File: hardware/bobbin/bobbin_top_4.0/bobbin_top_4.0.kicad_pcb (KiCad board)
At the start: 2 copper layers, 90.5 x 8.5 mm, 1 part

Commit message: new scheme
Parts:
- H3: footprint cycfi_library:single-pad-10x2 -> cycfi_library:xr2-4.0-bobbin-top
- moved H3 2.60 mm to (134.0, 65.0)
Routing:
- net GND: track 0.00 -> 2.70 mm, vias 2 -> 1
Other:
- outline, holes or cut-outs redrawn
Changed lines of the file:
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@@
   (general
     (thickness 1.6)
-    (drawings 20)
+    (drawings 12)
     (tracks 2)
     (zones 0)
@@
     (44 Edge.Cuts user)
     (45 Margin user)
-    (46 B.CrtYd user hide)
-    (47 F.CrtYd user hide)
-    (48 B.Fab user hide)
-    (49 F.Fab user hide)
+    (46 B.CrtYd user)
+    (47 F.CrtYd user)
+    (48 B.Fab user)
+    (49 F.Fab user)
   )
   (setup
@@
     (add_net GND)
   )
-  (module cycfi_library:single-pad-10x2 (layer F.Cu)
-    (at 134 62.4)
-    (fp_text reference H3 (at 6.5 0.1) (layer F.SilkS) hide
+  (module cycfi_library:xr2-4.0-bobbin-top (layer F.Cu)
+    (at 134 65)
+    (fp_text reference H3 (at 0 6) (layer F.SilkS)
       (effects (font (size 1 1) (thickness 0.15)))
     )
-    (fp_text value single_pad_smd (at 0 -2.54) (layer F.Fab)
+    (fp_text value single_pad_smd (at 0 -4) (layer F.Fab)
       (effects (font (size 1 1) (thickness 0.15)))
     )
-    (pad 1 smd rect (at 0 0) (size 10 2) (layers F.Cu F.Paste F.Mask)
+    (pad 1 thru_hole oval (at 0 0) (size 84.5 2.5) (drill oval 84 2) (layers *.Cu *.Mask)
       (net 1 GND))
   )
-  (gr_line (start 129 61.4) (end 129 63.4) (layer Dwgs.User) (width 0.05))
-  (gr_line (start 129 63.4) (end 139 63.4) (layer Dwgs.User) (width 0.05))
-  (gr_line (start 139 63.4) (end 139 61.4) (layer Dwgs.User) (width 0.05))
-  (gr_line (start 139 61.4) (end 129 61.4) (layer Dwgs.User) (width 0.05))
   (gr_arc (start 175 65) (end 175 69.25) (angle -180) (layer Edge.Cuts) (width 0.05))
-  (gr_line (start 175 64) (end 175 66) (layer Edge.Cuts) (width 0.05))
-  (gr_line (start 93 66) (end 175 66) (layer Edge.Cuts) (width 0.05))
-  (gr_line (start 93 64) (end 93 66) (layer Edge.Cuts) (width 0.05))
-  (gr_line (start 93 64) (end 175 64) (layer Edge.Cuts) (width 0.05))
   (gr_line (start 175 69.25) (end 93 69.25) (layer Edge.Cuts) (width 0.05))
   (gr_line (start 93 60.75) (end 175 60.75) (layer Edge.Cuts) (width 0.05))
   (gr_arc (start 93 65) (end 93 60.75) (angle -180) (layer Edge.Cuts) (width 0.05))
-  (gr_line (start 93 64) (end 93 66) (layer Dwgs.User) (width 0.05))
-  (gr_line (start 175 64) (end 175 66) (layer Dwgs.User) (width 0.05))
-  (gr_line (start 93 66) (end 175 66) (layer Dwgs.User) (width 0.05))
-  (gr_line (start 93 64) (end 175 64) (layer Dwgs.User) (width 0.05))
+  (gr_line (start 104 64) (end 104 66) (layer Dwgs.User) (width 0.05))
+  (gr_line (start 164 64) (end 164 66) (layer Dwgs.User) (width 0.05))
+  (gr_line (start 104 66) (end 164 66) (layer Dwgs.User) (width 0.05))
+  (gr_line (start 104 64) (end 164 64) (layer Dwgs.User) (width 0.05))
   (gr_line (start 175 69.25) (end 93 69.25) (layer Dwgs.User) (width 0.05))
   (gr_line (start 93 60.75) (end 175 60.75) (layer Dwgs.User) (width 0.05))
   (gr_arc (start 93 65) (end 93 60.75) (angle -180) (layer Dwgs.User) (width 0.05))
   (gr_arc (start 175 65) (end 175 69.25) (angle -180) (layer Dwgs.User) (width 0.05))
-  (via (at 128 62.5) (size 0.8) (drill 0.4) (layers F.Cu B.Cu) (net 1))
-  (via (at 140 62.5) (size 0.8) (drill 0.4) (layers F.Cu B.Cu) (net 1))
+  (via (at 134 62.3) (size 0.8) (drill 0.4) (layers F.Cu B.Cu) (net 1))
+  (segment (start 134 62.3) (end 134 65) (width 0.25) (layer B.Cu) (net 1))
   (zone (net 1) (net_name GND) (layer F.Cu) (hatch edge 0.508)
     (connect_pads yes (clearance 0.25))
@@
     (polygon
       (pts
-        (xy 180 70) (xy 88 70) (xy 88 60) (xy 180 60)
+        (xy 179.3 69.9) (xy 88.7 70) (xy 88.7 60) (xy 179.3 59.9)
       )
     )
@@
     (polygon
       (pts
-        (xy 180 70) (xy 88 70) (xy 88 60) (xy 180 60)
+        (xy 179.3 69.9) (xy 88.7 70) (xy 88.7 60) (xy 179.3 59.9)
       )
     )

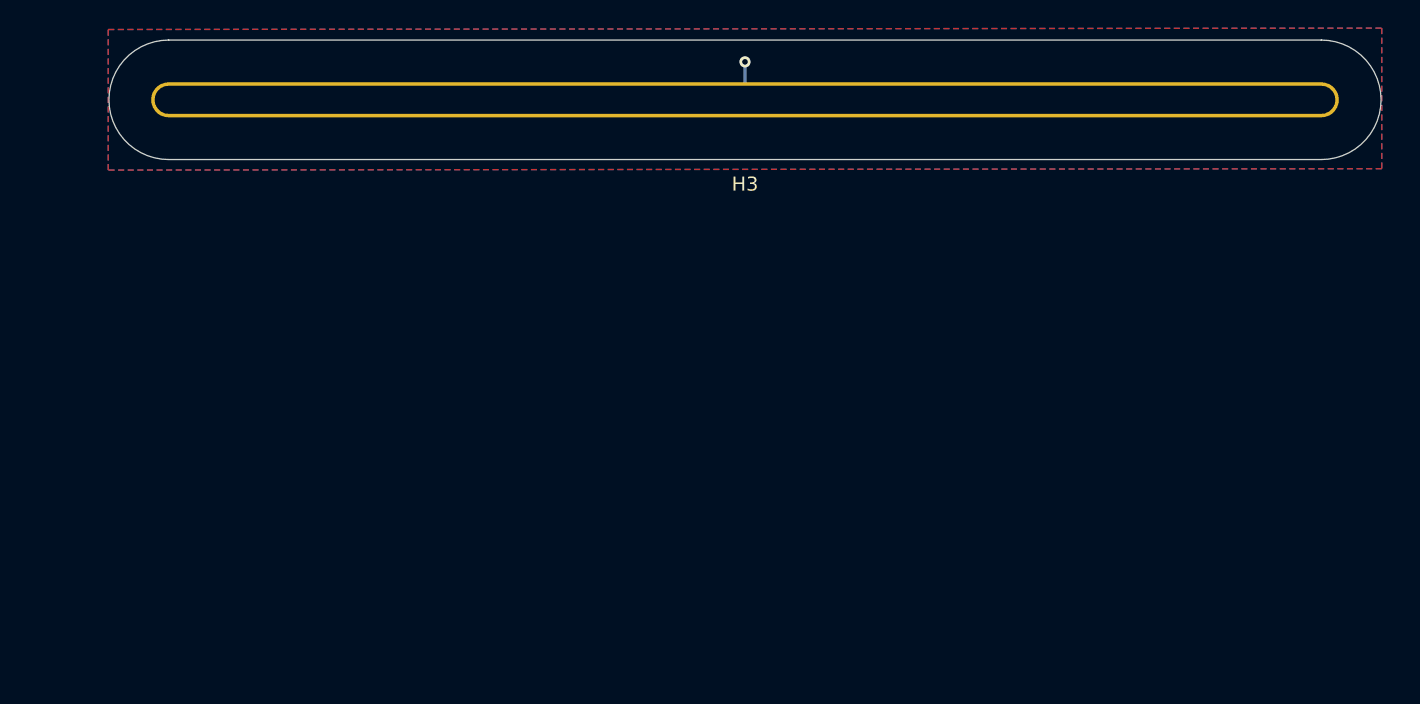
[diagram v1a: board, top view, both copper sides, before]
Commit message: Copied over bobbin_bottom to bobbin_top
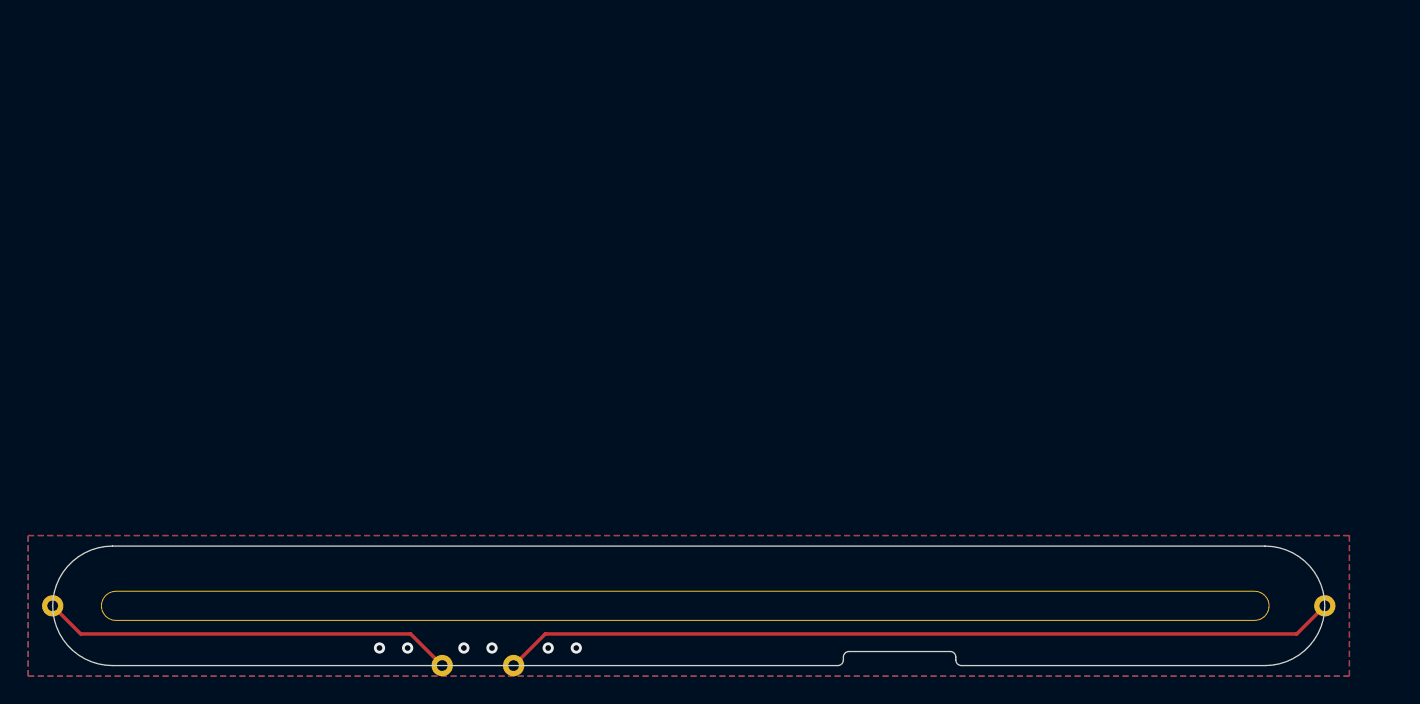
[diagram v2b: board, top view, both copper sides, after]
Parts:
- removed H3: single_pad_smd, cycfi_library:xr2-4.0-bobbin-top
- added H1: single_pad, xr_spectra_library:rail_slot_4.0, F.Cu at (129.8, 101.0)
- added J1: OC, cycfi_library:single-pad-1.52x1.52-th, F.Cu at (117.5, 105.2)
- added J2: OC, cycfi_library:single-pad-1.52x1.52-th, F.Cu at (175.2, 101.0)
- added J3: IC, cycfi_library:single-pad-1.52x1.52-th, F.Cu at (84.8, 101.0)
- added J4: IC, cycfi_library:single-pad-1.52x1.52-th, F.Cu at (112.5, 105.2)
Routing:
- net /OC: track 0.00 -> 59.5 mm
- net /IC: track 0.00 -> 29.5 mm
- net GND: track 2.70 -> 0.00 mm, vias 1 -> 6
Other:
- outline, holes or cut-outs redrawn
- net class Default removed

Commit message: Bobbin-top done
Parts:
- removed J1, J2: OC, cycfi_library:single-pad-1.52x1.52-th
- removed J3, J4: IC, cycfi_library:single-pad-1.52x1.52-th
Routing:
- net /OC: track 59.5 -> 0.00 mm
- net /IC: track 29.5 -> 0.00 mm
- net GND: vias 6 -> 0
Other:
- outline, holes or cut-outs redrawn
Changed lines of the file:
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@@
   (net 0 "")
   (net 1 "GND")
-  (net 2 "/OC")
-  (net 3 "/IC")
-  (footprint "cycfi_library:single-pad-1.52x1.52-th" (layer "F.Cu")
-    (at 117.54 105.25 180)
-    (property "Sheetfile" "bobbin_bottom_4.0.kicad_sch")
-    (property "Sheetname" "")
-    (attr through_hole)
-    (fp_text reference "J1" (at 0 2.54 180) (layer "F.SilkS") hide
-      (effects (font (size 1 1) (thickness 0.15)))
-    )
-    (fp_text value "OC" (at 0 -2.54 180) (layer "F.Fab")
-      (effects (font (size 1 1) (thickness 0.15)))
-    )
-    (pad "1" thru_hole circle (at 0 0 180) (size 1.52 1.52) (drill 0.76) (layers *.Cu *.Mask)
-      (net 2 "/OC") (pinfunction "Pin_1") (pintype "passive"))
-  )
-  (footprint "cycfi_library:single-pad-1.52x1.52-th" (layer "F.Cu")
-    (at 175.25 101 180)
-    (property "Sheetfile" "bobbin_bottom_4.0.kicad_sch")
-    (property "Sheetname" "")
-    (attr through_hole)
-    (fp_text reference "J2" (at 0 2.54) (layer "F.SilkS") hide
-      (effects (font (size 1 1) (thickness 0.15)))
-    )
-    (fp_text value "OC" (at -3 -0.09) (layer "F.Fab")
-      (effects (font (size 1 1) (thickness 0.15)))
-    )
-    (pad "1" thru_hole circle (at 0 0 180) (size 1.52 1.52) (drill 0.76) (layers *.Cu *.Mask)
-      (net 2 "/OC") (pinfunction "Pin_1") (pintype "passive"))
-  )
-  (footprint "cycfi_library:single-pad-1.52x1.52-th" (layer "F.Cu")
-    (at 84.75 101)
-    (property "Sheetfile" "bobbin_bottom_4.0.kicad_sch")
-    (property "Sheetname" "")
-    (attr through_hole)
-    (fp_text reference "J3" (at 0 2.54) (layer "F.SilkS") hide
-      (effects (font (size 1 1) (thickness 0.15)))
-    )
-    (fp_text value "IC" (at -2.75 0.08) (layer "F.Fab")
-      (effects (font (size 1 1) (thickness 0.15)))
-    )
-    (pad "1" thru_hole circle (at 0 0) (size 1.52 1.52) (drill 0.76) (layers *.Cu *.Mask)
-      (net 3 "/IC") (pinfunction "Pin_1") (pintype "passive"))
-  )
   (footprint "xr_spectra_library:rail_slot_4.0" (layer "F.Cu")
     (at 129.75 101)
-    (property "Sheetfile" "bobbin_bottom_4.0.kicad_sch")
+    (property "Sheetfile" "bobbin_top_4.0.kicad_sch")
     (property "Sheetname" "")
     (attr through_hole)
@@
     (pad "1" thru_hole oval (at 0 0) (size 83.15 2.15) (drill oval 83 2) (layers *.Cu *.Mask)
       (net 1 "GND") (pinfunction "1") (pintype "input"))
-  )
-  (footprint "cycfi_library:single-pad-1.52x1.52-th" (layer "F.Cu")
-    (at 112.46 105.25)
-    (property "Sheetfile" "bobbin_bottom_4.0.kicad_sch")
-    (property "Sheetname" "")
-    (attr through_hole)
-    (fp_text reference "J4" (at 0 2.54) (layer "F.SilkS") hide
-      (effects (font (size 1 1) (thickness 0.15)))
-    )
-    (fp_text value "IC" (at 0 2.25) (layer "F.Fab")
-      (effects (font (size 1 1) (thickness 0.15)))
-    )
-    (pad "1" thru_hole circle (at 0 0) (size 1.52 1.52) (drill 0.76) (layers *.Cu *.Mask)
-      (net 3 "/IC") (pinfunction "Pin_1") (pintype "passive"))
   )
   (gr_line (start 171 100) (end 171 102) (layer "Dwgs.User") (width 0.01))
@@
   (gr_arc (start 148.6 104.25) (mid 148.882843 104.367157) (end 149 104.65) (layer "Dwgs.User") (width 0.01))
   (gr_arc (start 84.818311 100.241068) (mid 85.512 101) (end 84.818311 101.758932) (layer "Dwgs.User") (width 0.01))
-  (gr_line (start 149 104.65) (end 149 104.85) (layer "Edge.Cuts") (width 0.01))
-  (gr_arc (start 141 104.85) (mid 140.882843 105.132843) (end 140.6 105.25) (layer "Edge.Cuts") (width 0.01))
-  (gr_line (start 140.6 105.25) (end 89 105.25) (layer "Edge.Cuts") (width 0.01))
-  (gr_arc (start 149.4 105.25) (mid 149.117157 105.132843) (end 149 104.85) (layer "Edge.Cuts") (width 0.01))
-  (gr_line (start 141.4 104.25) (end 148.6 104.25) (layer "Edge.Cuts") (width 0.01))
+  (gr_line (start 171 105.25) (end 89 105.25) (layer "Edge.Cuts") (width 0.01))
   (gr_line (start 89 96.75) (end 171 96.75) (layer "Edge.Cuts") (width 0.01))
-  (gr_line (start 171 105.25) (end 149.4 105.25) (layer "Edge.Cuts") (width 0.01))
-  (gr_arc (start 141 104.65) (mid 141.117157 104.367157) (end 141.4 104.25) (layer "Edge.Cuts") (width 0.01))
-  (gr_arc (start 148.6 104.25) (mid 148.882843 104.367157) (end 149 104.65) (layer "Edge.Cuts") (width 0.01))
   (gr_arc (start 89 105.25) (mid 84.75 101) (end 89 96.75) (layer "Edge.Cuts") (width 0.01))
-  (gr_line (start 141 104.85) (end 141 104.65) (layer "Edge.Cuts") (width 0.01))
   (gr_arc (start 171 96.75) (mid 175.25 101) (end 171 105.25) (layer "Edge.Cuts") (width 0.01))
-  (via (at 120 104) (size 0.8) (drill 0.4) (layers "F.Cu" "B.Cu") (free) (net 1))
-  (via (at 122 104) (size 0.8) (drill 0.4) (layers "F.Cu" "B.Cu") (free) (net 1))
-  (via (at 116 104) (size 0.8) (drill 0.4) (layers "F.Cu" "B.Cu") (free) (net 1))
-  (via (at 108 104) (size 0.8) (drill 0.4) (layers "F.Cu" "B.Cu") (free) (net 1))
-  (via (at 110 104) (size 0.8) (drill 0.4) (layers "F.Cu" "B.Cu") (free) (net 1))
-  (via (at 114 104) (size 0.8) (drill 0.4) (layers "F.Cu" "B.Cu") (free) (net 1))
-  (segment (start 173.25 103) (end 119.79 103) (width 0.25) (layer "F.Cu") (net 2))
-  (segment (start 119.79 103) (end 117.54 105.25) (width 0.25) (layer "F.Cu") (net 2))
-  (segment (start 175.25 101) (end 173.25 103) (width 0.25) (layer "F.Cu") (net 2))
-  (segment (start 84.75 101) (end 86.75 103) (width 0.25) (layer "F.Cu") (net 3))
-  (segment (start 86.75 103) (end 110.21 103) (width 0.25) (layer "F.Cu") (net 3))
-  (segment (start 110.21 103) (end 112.46 105.25) (width 0.25) (layer "F.Cu") (net 3))
   (zone (net 1) (net_name "GND") (layer "F.Cu") (hatch edge 0.508)
     (connect_pads (clearance 0.25))
